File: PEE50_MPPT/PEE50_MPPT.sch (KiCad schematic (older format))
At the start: 48 parts, among them J1 PV_IN1, J2 PV_IN2, J3 Conn_01x02_Female, J4 Vout, J5 PV_IN4, J6 PV_IN3, Q1 BC547, Q2 BC547, Q3 BC547, Q4 BC547, U1 LM3480-3.3, U24 NTA4151PT1G

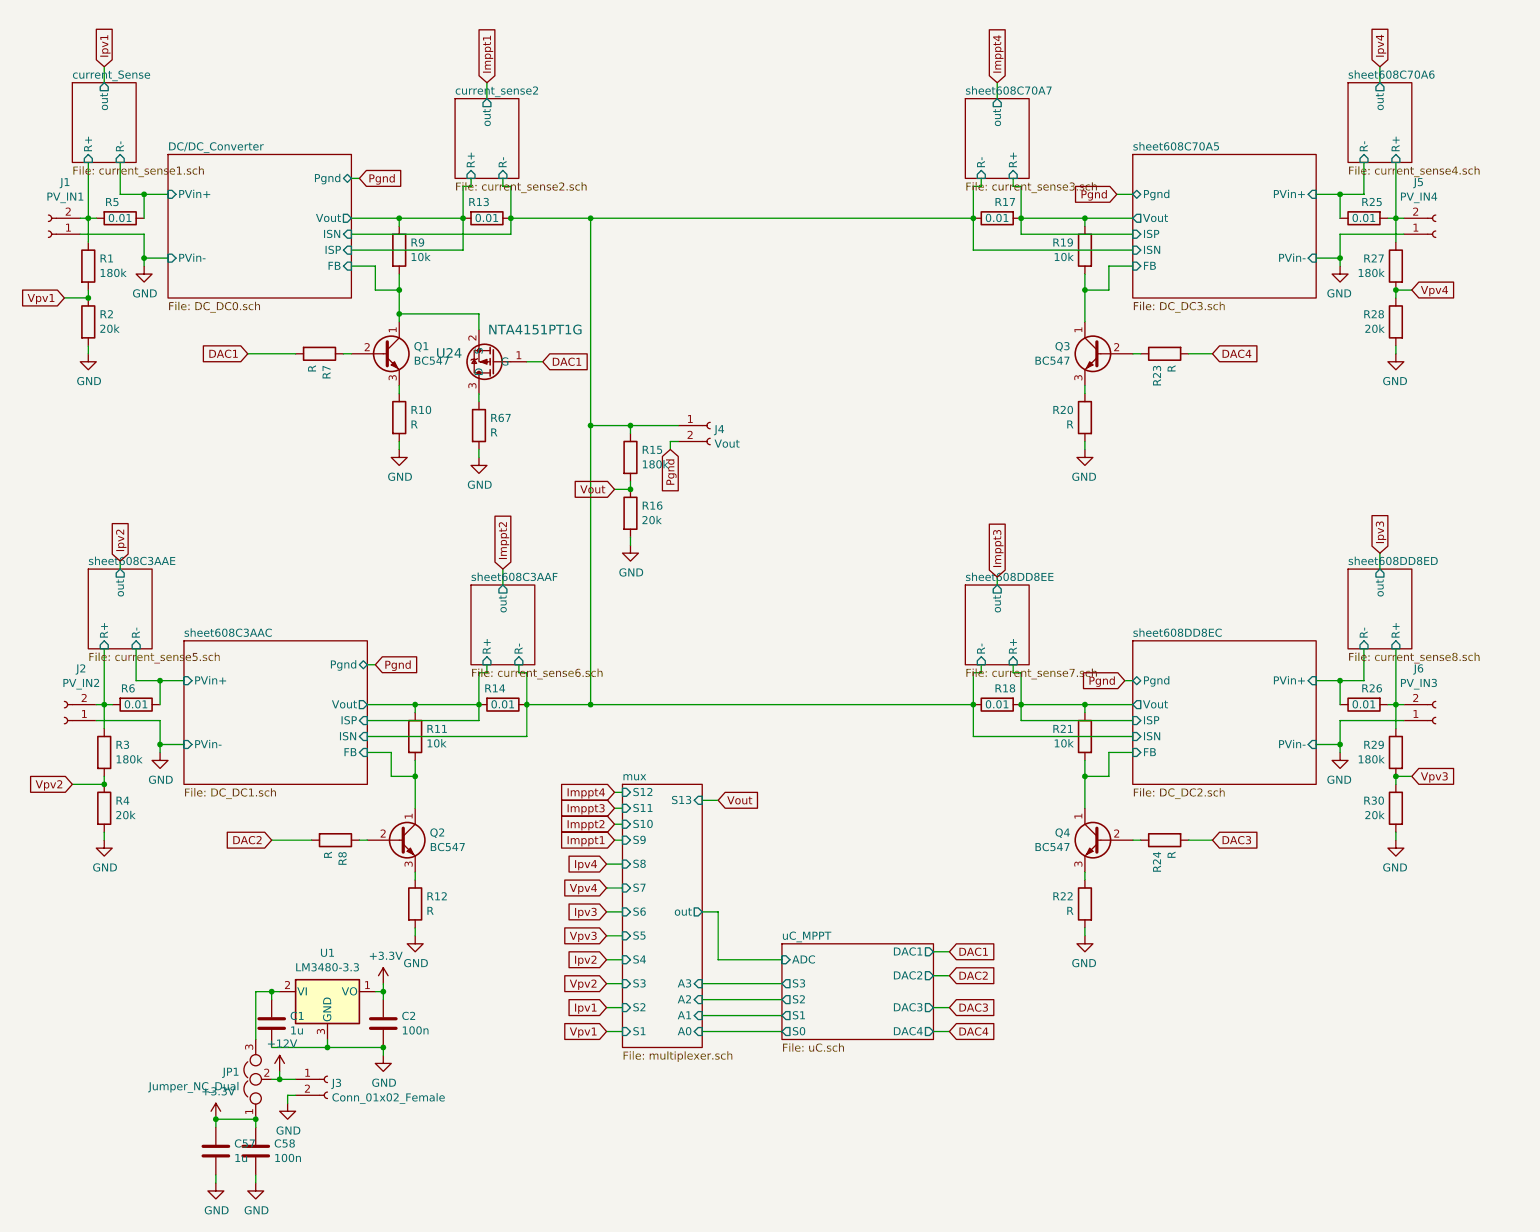
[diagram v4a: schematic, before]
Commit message: maar opnieuw begonnen met mppt layouten ivm plugin regels
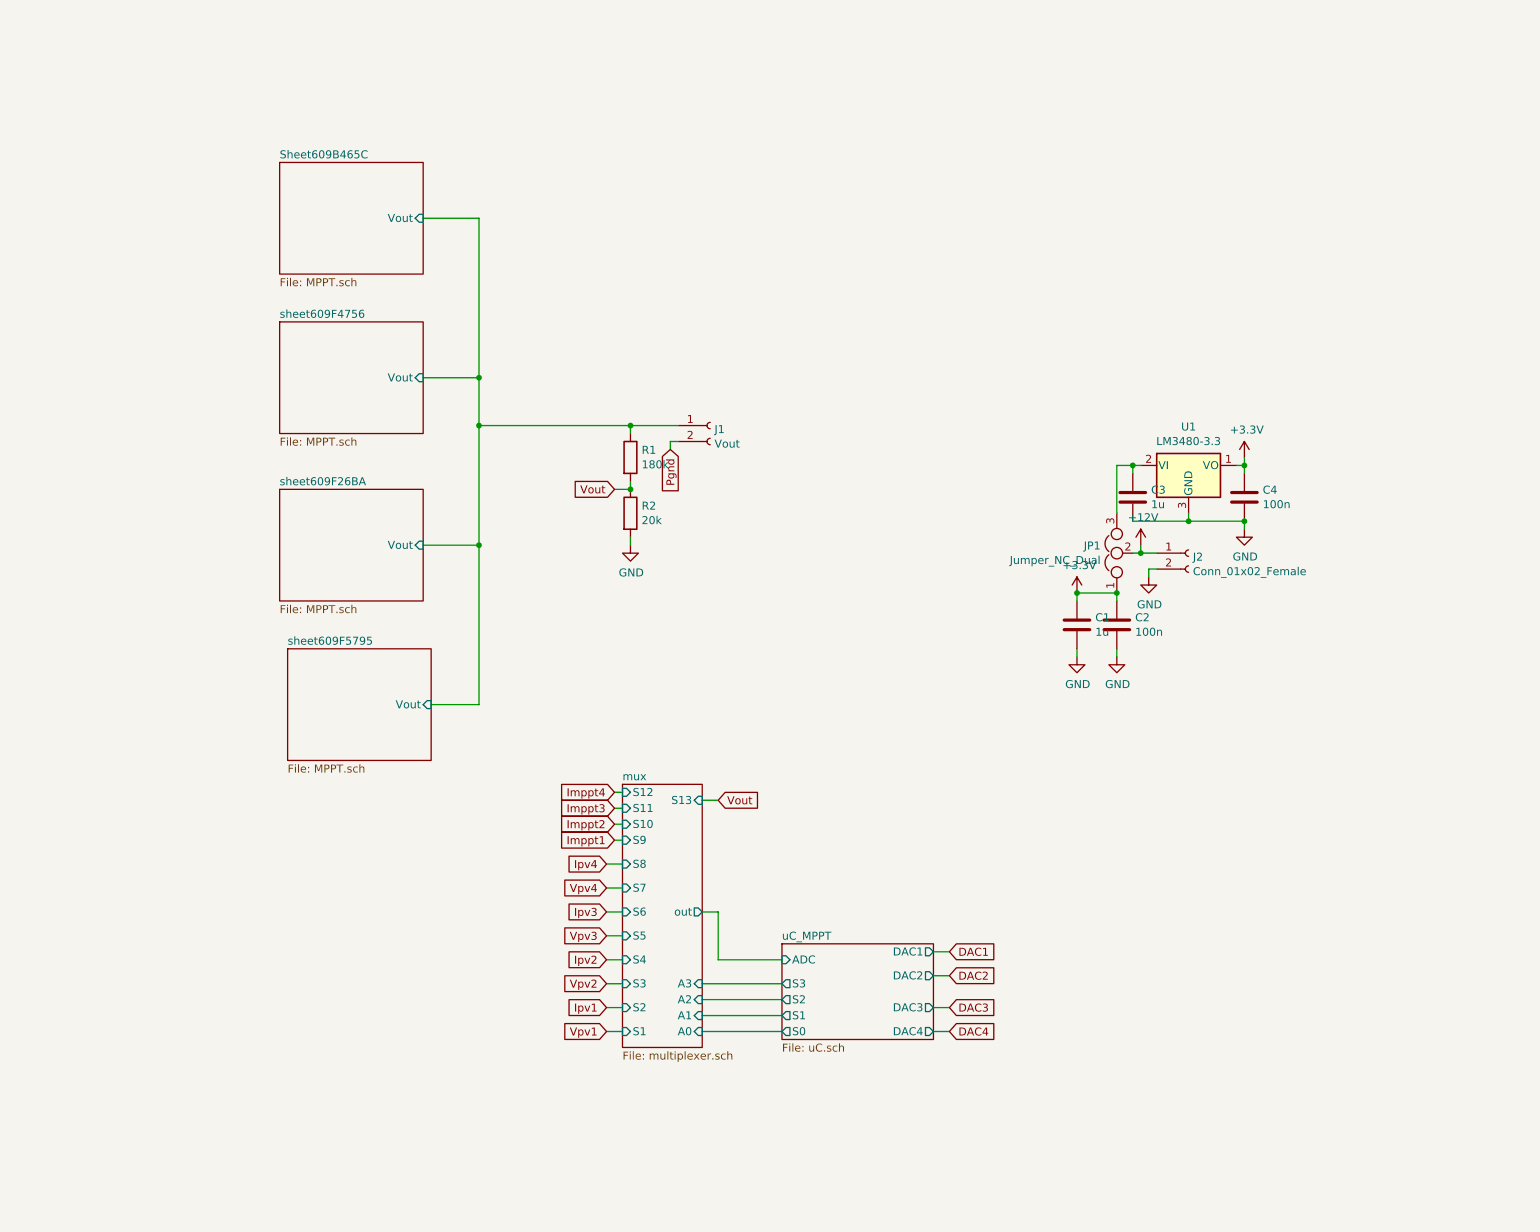
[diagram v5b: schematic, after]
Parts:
- removed J1: PV_IN1, Connector_Phoenix_MSTB:PhoenixContact_MSTBA_2,5_2-G-5,08_1x02_P5.08mm_Horizontal, symbol Connector:Conn_01x02_Female
- removed J2: PV_IN2, Connector_Phoenix_MSTB:PhoenixContact_MSTBA_2,5_2-G-5,08_1x02_P5.08mm_Horizontal, symbol Connector:Conn_01x02_Female
- removed J5: PV_IN4, Connector_Phoenix_MSTB:PhoenixContact_MSTBA_2,5_2-G-5,08_1x02_P5.08mm_Horizontal, symbol Connector:Conn_01x02_Female
- removed J6: PV_IN3, Connector_Phoenix_MSTB:PhoenixContact_MSTBA_2,5_2-G-5,08_1x02_P5.08mm_Horizontal, symbol Connector:Conn_01x02_Female
- removed Q1, Q2, Q3, Q4: BC547, Package_TO_SOT_THT:TO-92_Inline, symbol Transistor_BJT:BC547
- removed R1, R27, R29, R3: 180k, Resistor_SMD:R_1206_3216Metric_Pad1.42x1.75mm_HandSolder, symbol Device:R
- removed R10, R12, R20, R22, R23, R24, R67, R7, R8: R, Resistor_SMD:R_1206_3216Metric_Pad1.42x1.75mm_HandSolder, symbol Device:R
- removed R11, R19, R21, R9: 10k, Resistor_SMD:R_1206_3216Metric_Pad1.42x1.75mm_HandSolder, symbol Device:R
- removed R13, R14, R17, R18, R25, R26, R5, R6: 0.01, Resistor_SMD:R_2512_6332Metric_Pad1.52x3.35mm_HandSolder, symbol Device:R
- removed R2, R28, R30, R4: 20k, Resistor_SMD:R_1206_3216Metric_Pad1.42x1.75mm_HandSolder, symbol Device:R
- removed U24: NTA4151PT1G, AudioProject:NTA4151PT1G, symbol Robin_lib:NTA4151PT1G
- C3: renamed from C1; footprint AudioProject:CSD18543Q3A -> Capacitor_SMD:C_1206_3216Metric_Pad1.42x1.75mm_HandSolder
- renumbered C57 to C1, C58 to C2, C2 to C4, J4 to J1, J3 to J2, R15 to R1, R16 to R2
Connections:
- net DC/DC_Converter/ISN renamed Sheet609B465C/Vout
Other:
- moved on the sheet: C1, C2, C3, C4, J2, JP1, U1

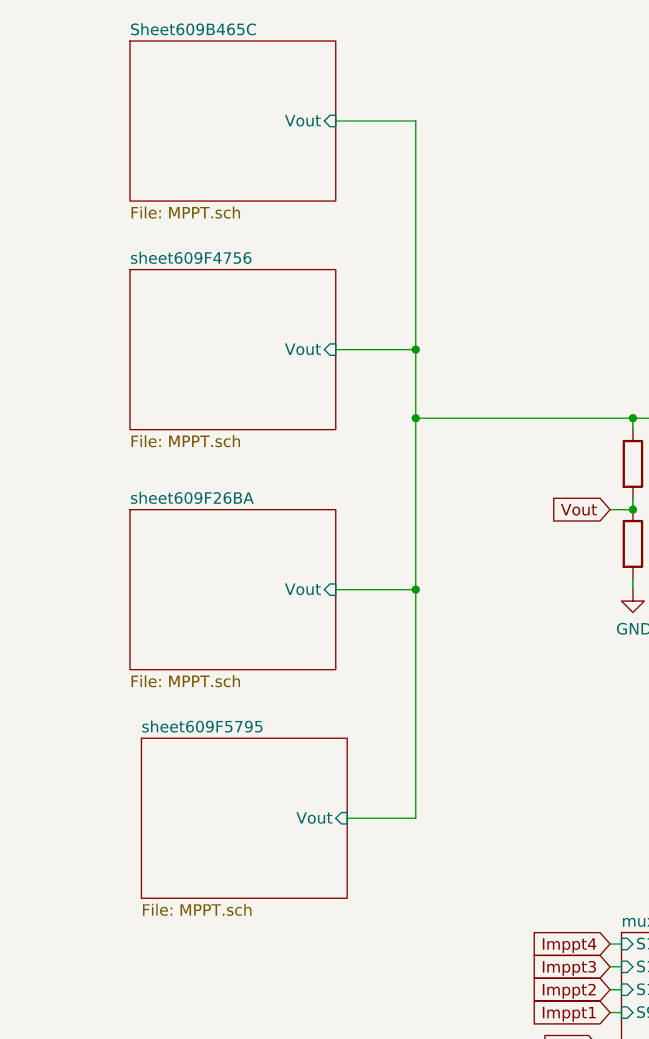
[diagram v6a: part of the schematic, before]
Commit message: spinneweb aangemaakt
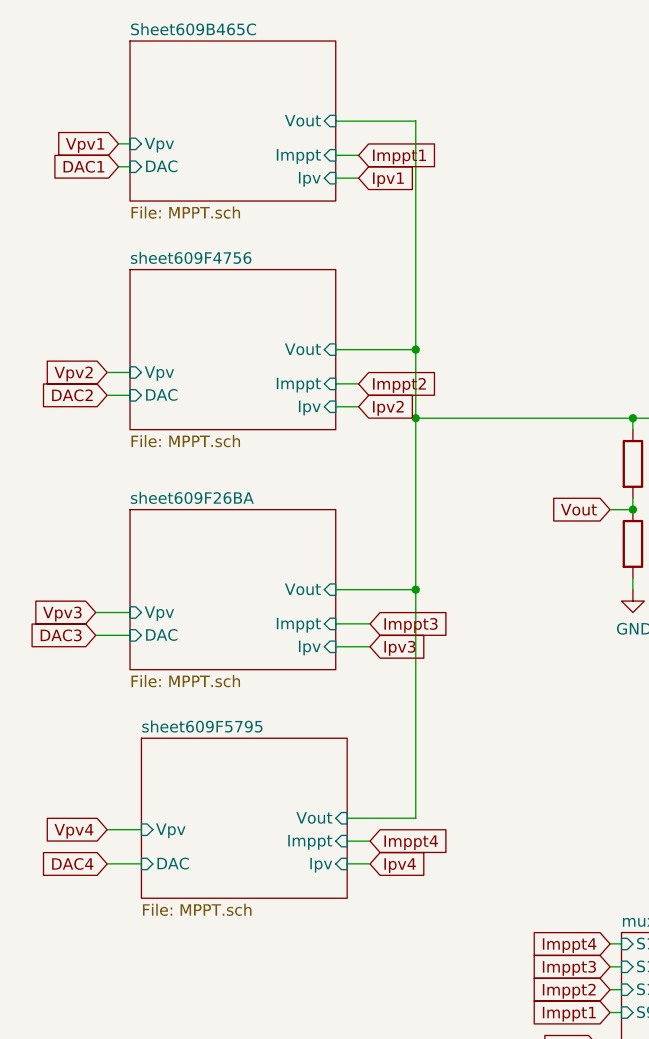
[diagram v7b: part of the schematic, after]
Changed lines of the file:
@@
 F1 "MPPT.sch" 50
 F2 "Vout" I R 3050 1750 50
+F3 "Imppt" I R 3050 1900 50
+F4 "Ipv" I R 3050 2000 50
+F5 "DAC" I L 2150 1950 50
+F6 "Vpv" I L 2150 1850 50
 $EndSheet
 $Sheet
@@
 F1 "MPPT.sch" 50
 F2 "Vout" I R 3050 3800 50
+F3 "Imppt" I R 3050 3950 50
+F4 "Ipv" I R 3050 4050 50
+F5 "DAC" I L 2150 4000 50
+F6 "Vpv" I L 2150 3900 50
 $EndSheet
 $Sheet
@@
 F1 "MPPT.sch" 50
 F2 "Vout" I R 3050 2750 50
+F3 "Imppt" I R 3050 2900 50
+F4 "Ipv" I R 3050 3000 50
+F5 "DAC" I L 2150 2950 50
+F6 "Vpv" I L 2150 2850 50
 $EndSheet
 $Sheet
@@
 F1 "MPPT.sch" 50
 F2 "Vout" I R 3100 4800 50
+F3 "Imppt" I R 3100 4900 50
+F4 "Ipv" I R 3100 5000 50
+F5 "DAC" I L 2200 5000 50
+F6 "Vpv" I L 2200 4850 50
 $EndSheet
 Wire Wire Line
@@
 Wire Wire Line
 	3400 3050 3400 3800
+Text GLabel 3150 1900 2    50   Input ~ 0
+Imppt1
+Text GLabel 3150 2000 2    50   Input ~ 0
+Ipv1
+Wire Wire Line
+	3050 1900 3150 1900
+Wire Wire Line
+	3050 2000 3150 2000
+Text GLabel 3150 2900 2    50   Input ~ 0
+Imppt2
+Text GLabel 3200 3950 2    50   Input ~ 0
+Imppt3
+Text GLabel 3200 4900 2    50   Input ~ 0
+Imppt4
+Text GLabel 3150 3000 2    50   Input ~ 0
+Ipv2
+Text GLabel 3200 4050 2    50   Input ~ 0
+Ipv3
+Text GLabel 3200 5000 2    50   Input ~ 0
+Ipv4
+Wire Wire Line
+	3150 2900 3050 2900
+Wire Wire Line
+	3050 3000 3150 3000
+Wire Wire Line
+	3200 3950 3050 3950
+Wire Wire Line
+	3050 4050 3200 4050
+Wire Wire Line
+	3200 4900 3100 4900
+Wire Wire Line
+	3100 5000 3200 5000
+Text GLabel 2100 1850 0    50   Input ~ 0
+Vpv1
+Text GLabel 2050 4850 0    50   Input ~ 0
+Vpv4
+Text GLabel 2000 3900 0    50   Input ~ 0
+Vpv3
+Text GLabel 2050 2850 0    50   Input ~ 0
+Vpv2
+Text GLabel 2100 1950 0    50   Input ~ 0
+DAC1
+Text GLabel 2050 2950 0    50   Input ~ 0
+DAC2
+Text GLabel 2000 4000 0    50   Input ~ 0
+DAC3
+Text GLabel 2050 5000 0    50   Input ~ 0
+DAC4
+Wire Wire Line
+	2050 5000 2200 5000
+Wire Wire Line
+	2050 4850 2200 4850
+Wire Wire Line
+	2000 4000 2150 4000
+Wire Wire Line
+	2000 3900 2150 3900
+Wire Wire Line
+	2050 2950 2150 2950
+Wire Wire Line
+	2050 2850 2150 2850
+Wire Wire Line
+	2100 1950 2150 1950
+Wire Wire Line
+	2100 1850 2150 1850
 $EndSCHEMATC

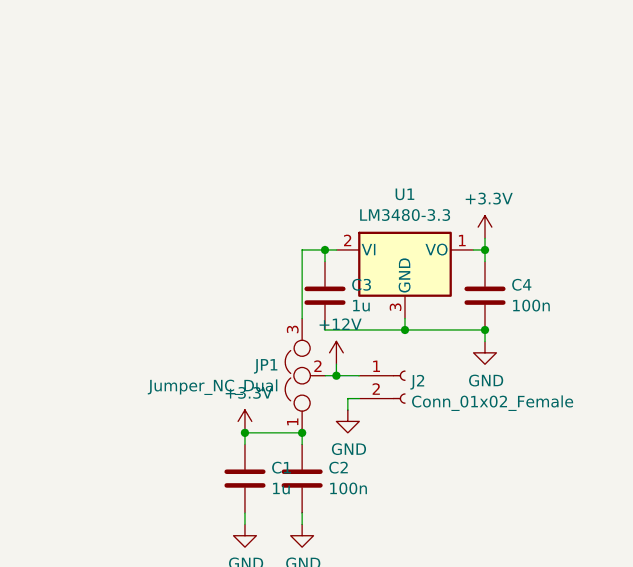
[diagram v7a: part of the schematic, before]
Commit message: reset pin en errors weggewerkt
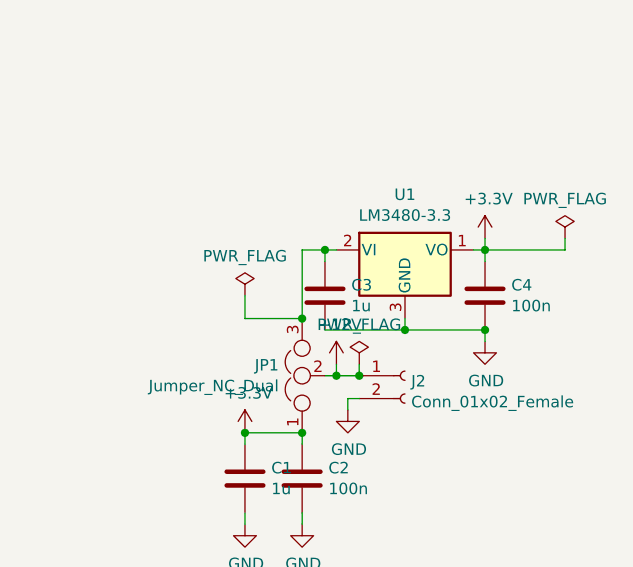
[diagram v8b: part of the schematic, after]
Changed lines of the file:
@@
 Wire Wire Line
 	2100 1850 2150 1850
+$Comp
+L power:PWR_FLAG #FLG0101
+U 1 1 60A43165
+P 8550 3250
+F 0 "#FLG0101" H 8550 3325 50  0001 C CNN
+F 1 "PWR_FLAG" H 8550 3423 50  0000 C CNN
+F 2 "" H 8550 3250 50  0001 C CNN
+F 3 "~" H 8550 3250 50  0001 C CNN
+	1    8550 3250
+	1    0    0    -1
+$EndComp
+Wire Wire Line
+	8550 3250 8550 3300
+Wire Wire Line
+	8550 3300 8200 3300
+Connection ~ 7400 3600
+Wire Wire Line
+	7150 3600 7400 3600
+Wire Wire Line
+	7150 3500 7150 3600
+$Comp
+L power:PWR_FLAG #FLG0102
+U 1 1 60A48B88
+P 7150 3500
+F 0 "#FLG0102" H 7150 3575 50  0001 C CNN
+F 1 "PWR_FLAG" H 7150 3673 50  0000 C CNN
+F 2 "" H 7150 3500 50  0001 C CNN
+F 3 "~" H 7150 3500 50  0001 C CNN
+	1    7150 3500
+	1    0    0    -1
+$EndComp
+$Comp
+L power:PWR_FLAG #FLG0103
+U 1 1 60A4C7DC
+P 7650 3800
+F 0 "#FLG0103" H 7650 3875 50  0001 C CNN
+F 1 "PWR_FLAG" H 7650 3973 50  0000 C CNN
+F 2 "" H 7650 3800 50  0001 C CNN
+F 3 "~" H 7650 3800 50  0001 C CNN
+	1    7650 3800
+	1    0    0    -1
+$EndComp
+Wire Wire Line
+	7650 3800 7650 3850
+Connection ~ 7650 3850
 $EndSCHEMATC
